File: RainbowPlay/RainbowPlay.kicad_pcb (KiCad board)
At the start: 2 copper layers, 140 x 80 mm, 23 parts, among them J1 GPIO_CONNECTOR, J2 PJ-102A, U1 LM386, U2 LM386

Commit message: Initial development in progress
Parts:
- removed C8: 250uF, Capacitor_THT:CP_Radial_D8.0mm_P5.00mm
- removed J2: PJ-102A, digikey-footprints:Barrel_Jack_5.5mmODx2.1mmID_PJ-102A
- removed LS1, LS2: Speaker, Connector_PinHeader_2.54mm:PinHeader_2x01_P2.54mm_Vertical
- removed MOD1: RN52-I_RM, kicad-footprints:rn52-breakout
- removed U2: LM386, Package_DIP:DIP-8_W7.62mm_Socket
- added D1: SK6812, LED_SMD:LED_SK6812_PLCC4_5.0x5.0mm_P3.2mm, F.Cu at (125.5, 68.8)
- added D10: SK6812, LED_SMD:LED_SK6812_PLCC4_5.0x5.0mm_P3.2mm, F.Cu at (177.3, 68.8)
- added D11: SK6812, LED_SMD:LED_SK6812_PLCC4_5.0x5.0mm_P3.2mm, F.Cu at (183.0, 68.8)
- added D12: SK6812, LED_SMD:LED_SK6812_PLCC4_5.0x5.0mm_P3.2mm, F.Cu at (188.8, 68.8)
- added D2: SK6812, LED_SMD:LED_SK6812_PLCC4_5.0x5.0mm_P3.2mm, F.Cu at (131.3, 68.8)
- added D3: SK6812, LED_SMD:LED_SK6812_PLCC4_5.0x5.0mm_P3.2mm, F.Cu at (137.0, 68.8)
- added D4: SK6812, LED_SMD:LED_SK6812_PLCC4_5.0x5.0mm_P3.2mm, F.Cu at (142.8, 68.8)
- added D5: SK6812, LED_SMD:LED_SK6812_PLCC4_5.0x5.0mm_P3.2mm, F.Cu at (148.5, 68.8)
- added D6: SK6812, LED_SMD:LED_SK6812_PLCC4_5.0x5.0mm_P3.2mm, F.Cu at (154.3, 68.8)
- added D7: SK6812, LED_SMD:LED_SK6812_PLCC4_5.0x5.0mm_P3.2mm, F.Cu at (160.0, 68.8)
- added D8: SK6812, LED_SMD:LED_SK6812_PLCC4_5.0x5.0mm_P3.2mm, F.Cu at (165.8, 68.8)
- added D9: SK6812, LED_SMD:LED_SK6812_PLCC4_5.0x5.0mm_P3.2mm, F.Cu at (171.5, 68.8)
- added L1: 10uH, Inductor_SMD:L_0603_1608Metric, B.Cu at (173.9, 100.4)
- added L2: 10uH, Inductor_SMD:L_0603_1608Metric, B.Cu at (171.4, 100.4)
- added Q1: BSS138, digikey-footprints:SOT-23-3, B.Cu at (171.3, 76.6)
- added Q2: BSS138, digikey-footprints:SOT-23-3, F.Cu at (120.3, 42.6)
- added R5: 10k, Resistor_SMD:R_0603_1608Metric, B.Cu at (175.0, 76.6)
- added R6: 10k, Resistor_SMD:R_0603_1608Metric, B.Cu at (165.5, 76.6)
- added R7: 330, Resistor_SMD:R_0603_1608Metric, F.Cu at (119.9, 46.3)
- added S1: GPTS203211B, digikey-footprints:PushButton_12x12mm_THT_GPTS203211B, F.Cu at (108.0, 42.0)
- added SWA1: B3F-3152, B3F-3152:B3F3152, F.Cu at (127.8, 117.3)
- added SWB1: B3F-3152, B3F-3152:B3F3152, F.Cu at (140.8, 117.3)
- added SWC1: B3F-3152, B3F-3152:B3F3152, F.Cu at (153.8, 117.3)
- added SWD1: B3F-3152, B3F-3152:B3F3152, F.Cu at (166.8, 117.3)
- added SWE1: B3F-3152, B3F-3152:B3F3152, F.Cu at (179.8, 117.3)
- added SWNT1: B3F-3152, B3F-3152:B3F3152, F.Cu at (197.5, 83.8)
- added SWPL1: B3F-3152, B3F-3152:B3F3152, F.Cu at (197.5, 96.8)
- added SWPT1: B3F-3152, B3F-3152:B3F3152, F.Cu at (197.5, 109.8)
- added SWVD1: B3F-3152, B3F-3152:B3F3152, F.Cu at (117.3, 102.3)
- added SWVU1: B3F-3152, B3F-3152:B3F3152, F.Cu at (117.3, 76.3)
- C1, C2: value 10uF -> 1.5uF; footprint Capacitor_THT:C_Disc_D3.4mm_W2.1mm_P2.50mm -> Capacitor_SMD:C_0603_1608Metric; moved to B.Cu
- C3: value 0.1uF -> 1uF; footprint Capacitor_THT:C_Disc_D3.4mm_W2.1mm_P2.50mm -> Capacitor_SMD:C_0603_1608Metric; moved to B.Cu
- C4: value 0.1uF -> 47nF; footprint Capacitor_THT:C_Disc_D3.4mm_W2.1mm_P2.50mm -> Capacitor_SMD:C_0603_1608Metric; moved to B.Cu
- C5, C6: value 0.05uF -> 47nF; footprint Capacitor_THT:C_Disc_D3.4mm_W2.1mm_P2.50mm -> Capacitor_SMD:C_0603_1608Metric; moved to B.Cu
- C7: value 250uF -> 47nF; footprint Capacitor_THT:CP_Radial_D8.0mm_P5.00mm -> Capacitor_SMD:C_0603_1608Metric; moved to B.Cu
- H1, H2, H3, H4: moved to B.Cu
- R1, R2: value 1.2k -> 5R; footprint Resistor_THT:R_Axial_DIN0204_L3.6mm_D1.6mm_P5.08mm_Horizontal -> Resistor_SMD:R_0603_1608Metric; moved to B.Cu
- R3, R4: value 10R -> 2.2k; footprint Resistor_THT:R_Axial_DIN0204_L3.6mm_D1.6mm_P5.08mm_Horizontal -> Resistor_SMD:R_0603_1608Metric; moved to B.Cu
- U1: value LM386 -> TPA2001D2; footprint Package_DIP:DIP-8_W7.62mm_Socket -> Package_SO:HTSSOP-24-1EP_4.4x7.8mm_P0.65mm_EP3.2x5mm; moved to B.Cu
- moved H1 105.4 mm to (186.3, 86.6), turned to 180 degrees
- moved H4 105.4 mm to (186.3, 109.6), turned to 180 degrees
- moved J1 53.3 mm to (133.2, 87.8)
- moved C5 37.0 mm to (167.0, 98.6), turned to 180 degrees
- moved C7 36.3 mm to (151.0, 96.8), turned to 180 degrees
- moved H2 36.1 mm to (128.3, 86.6), turned to 180 degrees
- moved H3 36.1 mm to (128.3, 109.6), turned to 180 degrees
- moved C6 33.1 mm to (151.8, 103.6), turned to 270 degrees
- moved C3 31.1 mm to (167.0, 100.8), turned to 180 degrees
- moved C1 30.3 mm to (151.0, 99.3)
- moved C4 29.5 mm to (167.0, 96.3), turned to 180 degrees
- moved U1 25.9 mm to (158.8, 98.8)
- moved R2 24.8 mm to (171.4, 96.4), turned to 90 degrees
- moved R4 24.2 mm to (167.0, 105.6)
- moved C2 23.9 mm to (172.8, 103.1)
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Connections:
- C1 pad 2: Net-(C1-Pad2) -> GNDA
- C2 pad 2: Net-(C2-Pad2) -> Net-(C1-Pad1)
- C3 pad 1: GNDA -> /MIC_BIAS
- C3 pad 2: Net-(C3-Pad2) -> GNDA
- C4 pad 1: GNDA -> /MIC_BIAS
- C4 pad 2: Net-(C4-Pad2) -> /MIC_R+
- C5 pad 1: Net-(C5-Pad1) -> /MIC_BIAS
- C5 pad 2: GNDA -> /MIC_L+
- C6 pad 1: Net-(C6-Pad1) -> /MIC_L-
- C6 pad 2: GNDA -> Net-(C2-Pad1)
- C7 pad 1: Net-(C7-Pad1) -> /MIC_R-
- C7 pad 2: Net-(C7-Pad2) -> Net-(C1-Pad1)
- J1 pad 10: /GPIO15_RXD0 -> (no net)
- J1 pad 12: (no net) -> /LED
- J1 pad 16: (no net) -> /BTN_A
- J1 pad 17: +3V3 -> (no net)
- J1 pad 18: (no net) -> /BTN_B
- J1 pad 2: +15V -> +5V
- J1 pad 20: (no net) -> GND
- J1 pad 27: (no net) -> /BTN_C
- J1 pad 29: (no net) -> /BTN_D
- J1 pad 31: (no net) -> /BTN_E
- J1 pad 32: (no net) -> /PWM_AUDIO_L
- J1 pad 33: (no net) -> /PWM_AUDIO_R
- J1 pad 39: GND -> (no net)
- J1 pad 4: +15V -> +5V
- J1 pad 40: (no net) -> /PWR_BTN
- J1 pad 8: /GPIO14_TXD0 -> (no net)
- R1 pad 1: Net-(R1-Pad1) -> Net-(L1-Pad1)
- R1 pad 2: Net-(C1-Pad2) -> /PWM_AUDIO_R
- R2 pad 2: Net-(C2-Pad2) -> /PWM_AUDIO_L
- R3 pad 1: Net-(C7-Pad1) -> Net-(C1-Pad1)
- R3 pad 2: Net-(C5-Pad1) -> /MIC_BIAS
- R4 pad 1: Net-(C8-Pad1) -> Net-(C2-Pad1)
- R4 pad 2: Net-(C6-Pad1) -> /MIC_BIAS
- U1 pad 1: Net-(R1-Pad1) -> GNDPWR
- U1 pad 2: /SPK_R- -> (no net)
- U1 pad 3: /SPK_R+ -> (no net)
- U1 pad 4: GNDA -> (no net)
- U1 pad 5: Net-(C7-Pad1) -> /MIC_L-
- U1 pad 6: +15V -> GNDA
- U1 pad 7: Net-(C3-Pad2) -> (no net)
- U1 pad 8: Net-(C1-Pad1) -> /MIC_R-
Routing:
- added copper zone on In2.Cu, net GND
- removed copper zone on F.Cu, net GND
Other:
- board size 140 x 80 mm -> 90 x 58.2 mm
- copper layers 2 -> 4
- board text removed: "Board Corner Radius = 3mm All holes are M2.5"

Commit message: Development
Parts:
- removed SWNT1, SWPL1, SWPT1, SWVD1, SWVU1: B3F-3152, B3F-3152:B3F3152
- added J3: Conn_01x04_Male, Connector_PinHeader_2.54mm:PinHeader_1x04_P2.54mm_Vertical, F.Cu at (175.2, 42.2)
- added LS1: Speaker, Connector_PinHeader_2.54mm:PinHeader_1x02_P2.54mm_Vertical, F.Cu at (179.9, 42.2)
- added LS2: Speaker, Connector_PinHeader_2.54mm:PinHeader_1x02_P2.54mm_Vertical, F.Cu at (184.5, 42.2)
- added R8: 200R, Resistor_SMD:R_0603_1608Metric, F.Cu at (183.6, 53.3)
- C3: value 1uF -> 1.5uF; moved to F.Cu
- C4, C5: value 47nF -> 0.1uF; moved to F.Cu
- C6, C7: value 47nF -> 0.1uF
- R3, R4: value 2.2k -> 5R; moved to F.Cu
- R7: value 330 -> 120k
- S1: value GPTS203211B -> AB11AH-FA; footprint digikey-footprints:PushButton_12x12mm_THT_GPTS203211B -> magic-music-box:AB11AH-FA; moved to B.Cu
- moved R7 60.4 mm to (179.6, 55.8)
- moved R4 57.2 mm to (183.5, 50.8)
- moved Q2 56.2 mm to (175.2, 54.6)
- moved C3 54.0 mm to (179.5, 48.3), turned to 0 degrees
- moved R3 51.3 mm to (179.6, 53.3)
- moved C4 50.8 mm to (183.5, 48.3), turned to 0 degrees
- moved C5 49.3 mm to (179.5, 50.8), turned to 0 degrees
- moved S1 40.9 mm to (126.8, 78.3), turned to 180 degrees
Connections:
- net /MIC_L- renamed /AUD_L-
- net /MIC_R- renamed /AUD_R-
- C3 pad 1: /MIC_BIAS -> GNDA
- C3 pad 2: GNDA -> Net-(C2-Pad1)
- C4 pad 1: /MIC_BIAS -> /AUD_L+
- C4 pad 2: /MIC_R+ -> Net-(C2-Pad1)
- C5 pad 1: /MIC_BIAS -> /AUD_R+
- C5 pad 2: /MIC_L+ -> Net-(C1-Pad1)
- C6 pad 2: Net-(C2-Pad1) -> GNDA
- C7 pad 2: Net-(C1-Pad1) -> GNDA
- J1 pad 10: (no net) -> /UART_RX
- J1 pad 35: (no net) -> /GAIN_0
- J1 pad 36: (no net) -> /PWR_LED
- J1 pad 37: (no net) -> /GAIN_1
- J1 pad 8: (no net) -> /UART_TX
- Q2 pad 1: (no net) -> /PWR_LED
- Q2 pad 2: (no net) -> Net-(Q2-Pad2)
- R3 pad 1: Net-(C1-Pad1) -> GNDA
- R3 pad 2: /MIC_BIAS -> Net-(C1-Pad1)
- R4 pad 2: /MIC_BIAS -> GNDA
- R7 pad 1: (no net) -> GND
- R7 pad 2: (no net) -> Net-(R7-Pad2)
- U1 pad 1: GNDPWR -> GND
- U1 pad 10: (no net) -> +5V
- U1 pad 11: (no net) -> /SPK_R-
- U1 pad 12: GNDPWR -> GND
- U1 pad 13: GNDPWR -> GND
- U1 pad 14: (no net) -> /SPK_R+
- U1 pad 15: (no net) -> /GAIN_1
- U1 pad 16: (no net) -> +5V
- U1 pad 17: /MIC_R+ -> /AUD_R+
- U1 pad 18: (no net) -> Net-(R7-Pad2)
- U1 pad 19: (no net) -> +5V
- U1 pad 2: (no net) -> /SPK_L-
- U1 pad 20: /MIC_L+ -> /AUD_L+
- U1 pad 21: (no net) -> +5V
- U1 pad 23: (no net) -> /SPK_L+
- U1 pad 24: GNDPWR -> GND
- U1 pad 3: (no net) -> /GAIN_0
- U1 pad 4: (no net) -> +5V
- U1 pad 6: GNDA -> GND
- U1 pad 9: (no net) -> +5V

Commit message: Development
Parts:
- added C10: 220pF, Capacitor_SMD:C_0603_1608Metric, F.Cu at (216.5, 101.1)
- added C11: 0.1uF, Capacitor_SMD:C_0603_1608Metric, F.Cu at (236.3, 73.3)
- added C12: 0.1uF, Capacitor_SMD:C_0603_1608Metric, F.Cu at (224.3, 75.8)
- added C13: 0.1uF, Capacitor_SMD:C_0603_1608Metric, F.Cu at (230.3, 97.6)
- added C14: 1uF, Capacitor_SMD:C_0603_1608Metric, F.Cu at (230.3, 94.1)
- added C15: 10uF, Capacitor_SMD:C_0603_1608Metric, F.Cu at (230.3, 95.8)
- added C16: 10uF, Capacitor_SMD:C_0603_1608Metric, F.Cu at (234.3, 100.1)
- added C8: 0.1uF, Capacitor_SMD:C_0603_1608Metric, F.Cu at (214.3, 101.1)
- added C9: 0.1uF, Capacitor_SMD:C_0603_1608Metric, F.Cu at (214.3, 96.6)
- added D13: LED, LED_SMD:LED_0603_1608Metric, F.Cu at (198.5, 74.8)
- added J2: Conn_01x06_Male, Connector_PinHeader_2.54mm:PinHeader_1x06_P2.54mm_Vertical, F.Cu at (135.8, 79.8)
- C1, C2, C6, C7, L1, L2, R1, R2, U1: moved to F.Cu
- moved J3 77.6 mm to (117.5, 94.1)
- moved R7 66.9 mm to (230.3, 99.6), turned to 180 degrees
- moved U1 64.8 mm to (223.5, 98.1)
- moved C1 58.6 mm to (209.5, 96.8)
- moved C7 58.6 mm to (209.5, 99.3)
- moved C6 21.8 mm to (173.3, 100.1), turned to 90 degrees
- moved C2 11.0 mm to (181.0, 95.8)
- moved R1 10.4 mm to (182.1, 102.6), turned to 270 degrees
- moved R2 10.3 mm to (179.7, 102.5), turned to 270 degrees
- moved L1 8.45 mm to (182.1, 98.5), turned to 90 degrees
- moved L2 8.45 mm to (179.7, 98.5), turned to 90 degrees
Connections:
- J1 pad 38: (no net) -> /LB
- Q2 pad 3: (no net) -> Net-(D13-Pad1)
- U1 pad 22: (no net) -> Net-(C14-Pad2)
- U1 pad 7: (no net) -> Net-(C10-Pad2)

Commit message: Development
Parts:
- removed C2: 1.5uF, Capacitor_SMD:C_0603_1608Metric
- removed H3, H4: MountingHole, lib:MountingHole_2.7mm_M2.5_uHAT_RPi
- removed SWA1, SWB1, SWC1, SWD1, SWE1: B3F-3152, B3F-3152:B3F3152
- added D14: LED, LED_SMD:LED_0603_1608Metric, F.Cu at (100.2, 84.1)
- added D15: 1N5819HW-7-F, digikey-footprints:SOD-123, F.Cu at (90.5, 72.6)
- added D16: 1N5819HW-7-F, digikey-footprints:SOD-123, F.Cu at (91.0, 76.8)
- added J4: Conn_01x02_Male, Connector_PinHeader_2.54mm:PinHeader_1x02_P2.54mm_Vertical, F.Cu at (222.4, 84.0)
- added J5: Conn_01x02_Male, Connector_PinHeader_2.54mm:PinHeader_1x02_P2.54mm_Vertical, F.Cu at (227.1, 84.0)
- added J6: Conn_02x12_Odd_Even, Connector_PinSocket_2.54mm:PinSocket_2x12_P2.54mm_Vertical_SMD, F.Cu at (137.7, 79.1)
- added Q3: BSS138, digikey-footprints:SOT-23-3, F.Cu at (88.4, 91.9)
- added Q4: BSS138, digikey-footprints:SOT-23-3, F.Cu at (95.8, 90.2)
- added R10: 200R, Resistor_SMD:R_0603_1608Metric, F.Cu at (96.8, 93.9)
- added R11: 10k, Resistor_SMD:R_0603_1608Metric, F.Cu at (100.2, 89.1)
- added R12: 10k, Resistor_SMD:R_0603_1608Metric, F.Cu at (104.2, 86.5)
- added R9: 200k, Resistor_SMD:R_0603_1608Metric, F.Cu at (100.2, 86.6)
- added S2: B3F-4050, B3F-4050:SW_B3F-4050, F.Cu at (144.4, 112.1)
- added S3: B3F-4050, B3F-4050:SW_B3F-4050, F.Cu at (157.9, 112.1)
- added S4: B3F-4050, B3F-4050:SW_B3F-4050, F.Cu at (171.4, 112.1)
- added S5: B3F-4050, B3F-4050:SW_B3F-4050, F.Cu at (184.9, 112.1)
- added SW1: SW_SPST, Button_Switch_THT:SW_PUSH_6mm, F.Cu at (211.6, 83.7)
- added U2: SN74LVC1G32DBVRG4, Package_TO_SOT_SMD:SOT-23-5, F.Cu at (103.0, 95.1)
- C1, C10, C13, C14, C15, C16, C8, C9, J2, R7, U1: moved to B.Cu
- C4, C5, C6: value 0.1uF -> 10uF
- C7: value 0.1uF -> 10uF; moved to B.Cu
- J1: footprint lib:PinSocket_2x20_P2.54mm_Vertical_Centered_Anchor -> Connector_PinSocket_2.54mm:PinSocket_2x20_P2.54mm_Vertical_SMD
- R3, R4: value 5R -> 10k
- S1: value AB11AH-FA -> B3F-4050; footprint magic-music-box:AB11AH-FA -> B3F-4050:SW_B3F-4050; moved to F.Cu
- moved R3 95.8 mm to (92.8, 93.9)
- moved R4 86.0 mm to (104.2, 84.0)
- moved Q2 85.1 mm to (95.8, 85.2)
- moved Q1 84.6 mm to (108.9, 133.9)
- moved R5 84.6 mm to (112.7, 133.8)
- moved R6 84.6 mm to (103.2, 133.8)
- moved C3 81.5 mm to (209.9, 123.9)
- moved C4 81.5 mm to (213.9, 123.9)
- moved C5 81.5 mm to (209.9, 126.4)
- moved R8 81.5 mm to (214.0, 128.9)
- moved C16 58.2 mm to (180.9, 76.9), turned to 0 degrees
- moved H1 55.9 mm to (183.5, 30.7)
- moved H2 55.9 mm to (125.5, 30.7)
- moved L2 54.8 mm to (227.7, 125.0)
- moved R2 54.8 mm to (227.7, 129.0)
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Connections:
- C3 pad 2: Net-(C2-Pad1) -> Net-(C3-Pad2)
- C4 pad 2: Net-(C2-Pad1) -> Net-(C3-Pad2)
- C9 pad 2: GND -> GNDA
- J1 pad 28: (no net) -> /M1
- J1 pad 36: /PWR_LED -> /M2
- J1 pad 38: /LB -> /AWAKE_SIG
- J1 pad 40: /PWR_BTN -> (no net)
- J2 pad 2: GND -> (no net)
- J2 pad 3: /LB -> (no net)
- J2 pad 4: (no net) -> GND
- J2 pad 5: (no net) -> /PWR_EN
- J2 pad 6: (no net) -> /Vs
- L2 pad 2: Net-(C2-Pad1) -> Net-(C3-Pad2)
- Q2 pad 1: /PWR_LED -> +3V3
- Q2 pad 2: Net-(Q2-Pad2) -> /AWAKE_SIG
- Q2 pad 3: Net-(D13-Pad1) -> Net-(Q2-Pad3)
- R3 pad 1: GNDA -> GND
- R3 pad 2: Net-(C1-Pad1) -> /AWAKE_SIG
- R4 pad 1: Net-(C2-Pad1) -> Net-(R4-Pad1)
- R4 pad 2: GNDA -> /Vs
- R8 pad 2: Net-(Q2-Pad2) -> Net-(D13-Pad1)
- S1 pad 1: /PWR_BTN -> /BTN_A
- U1 pad 6: GND -> GNDA

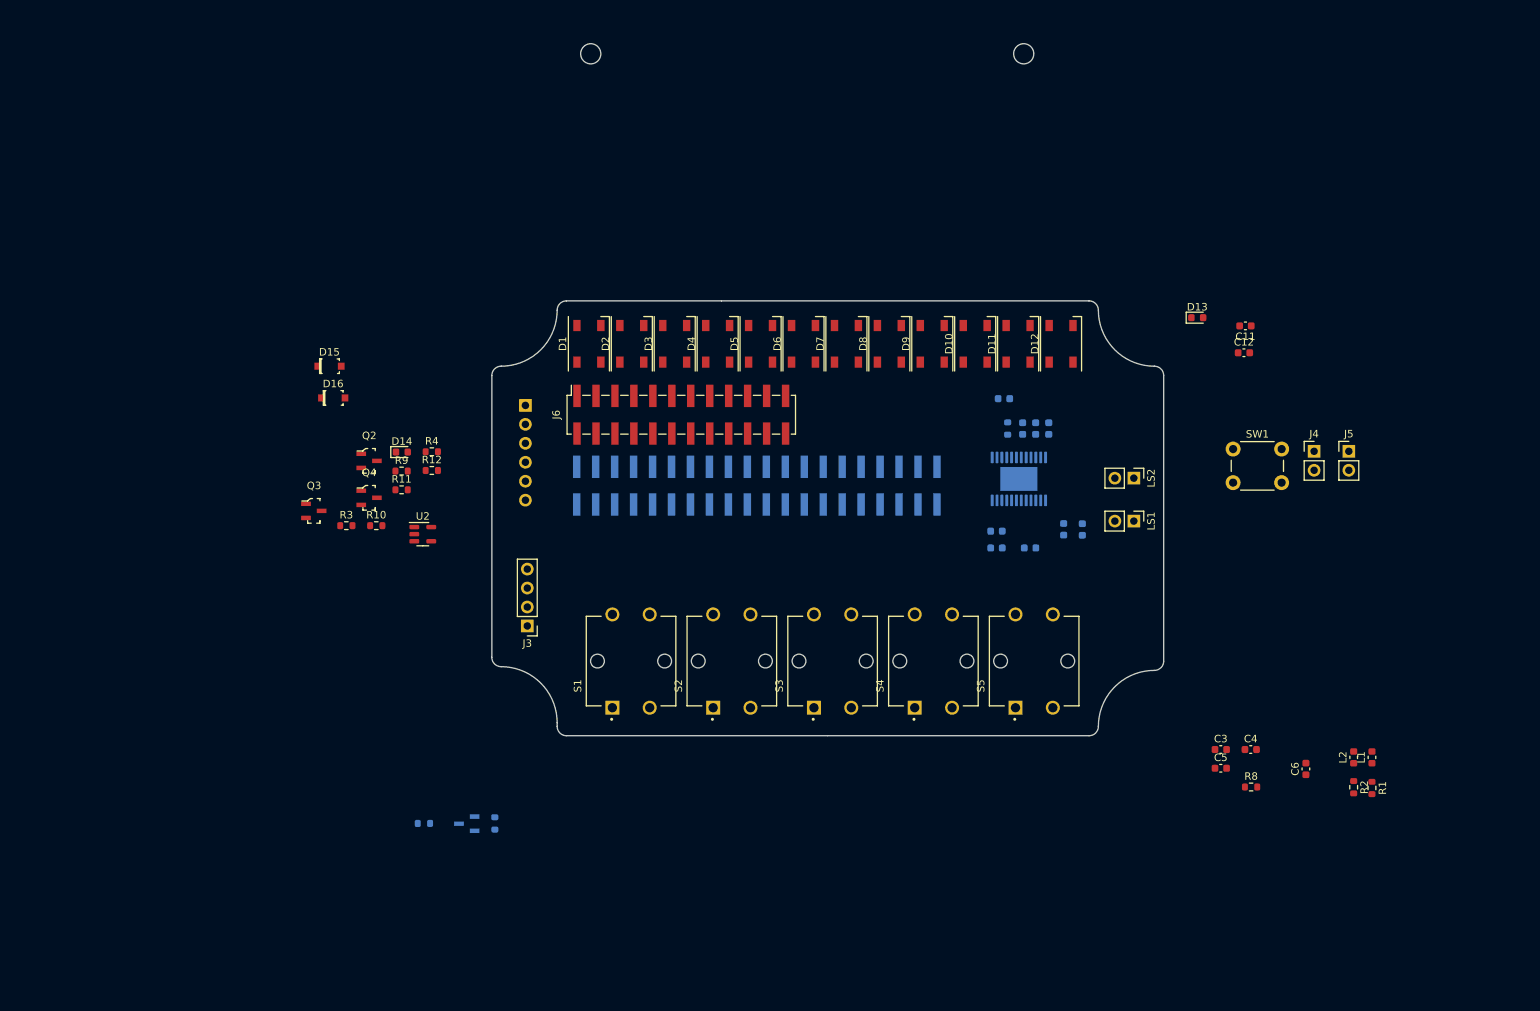
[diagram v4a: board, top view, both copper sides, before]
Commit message: PCB dev
- Work on power up, power down
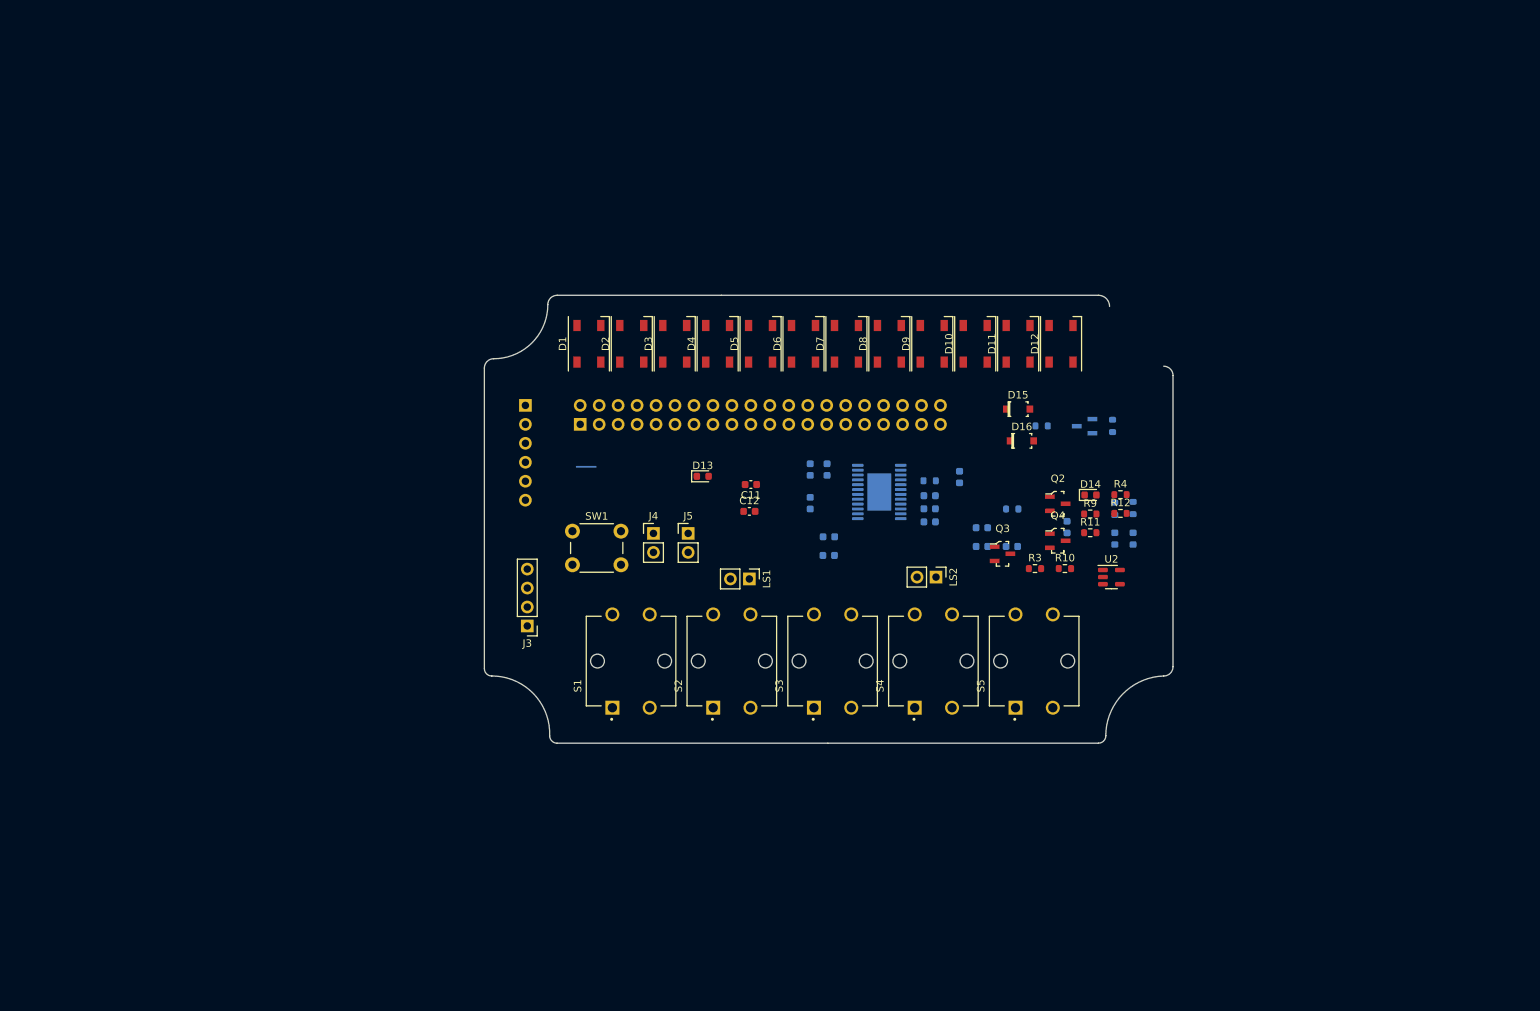
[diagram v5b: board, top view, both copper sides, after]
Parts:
- removed H1, H2: MountingHole, lib:MountingHole_2.7mm_M2.5_uHAT_RPi
- removed J6: Conn_02x12_Odd_Even, Connector_PinSocket_2.54mm:PinSocket_2x12_P2.54mm_Vertical_SMD
- C3, C4, C5, C6, L1, L2, R1, R2, R8: moved to B.Cu
- J1: footprint Connector_PinSocket_2.54mm:PinSocket_2x20_P2.54mm_Vertical_SMD -> Connector_PinSocket_2.54mm:PinSocket_2x20_P2.54mm_Vertical
- moved Q1 98.4 mm to (191.7, 80.6)
- moved R5 98.4 mm to (195.4, 80.6)
- moved R6 98.4 mm to (185.9, 80.6)
- moved D15 92.4 mm to (182.8, 78.3)
- moved D16 92.4 mm to (183.3, 82.6)
- moved Q3 92.4 mm to (180.7, 97.7)
- moved R11 92.4 mm to (192.4, 94.9)
- moved R9 92.4 mm to (192.4, 92.4)
- moved U2 92.4 mm to (195.3, 100.8)
- moved D14 92.4 mm to (192.5, 89.8)
- moved R3 92.4 mm to (185.0, 99.7)
- moved Q2 92.4 mm to (188.1, 91.0)
- moved Q4 92.4 mm to (188.1, 95.9)
- moved R10 92.4 mm to (189.1, 99.7)
- moved R12 92.4 mm to (196.5, 92.3)
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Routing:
- net +5V: track 0.00 -> 2.54 mm
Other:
- board size 90 x 58.2 mm -> 92.3 x 60 mm
